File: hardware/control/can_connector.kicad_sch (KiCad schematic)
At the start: 2 parts, among them J401 RJ45_Shielded, J402 RJ45_Shielded

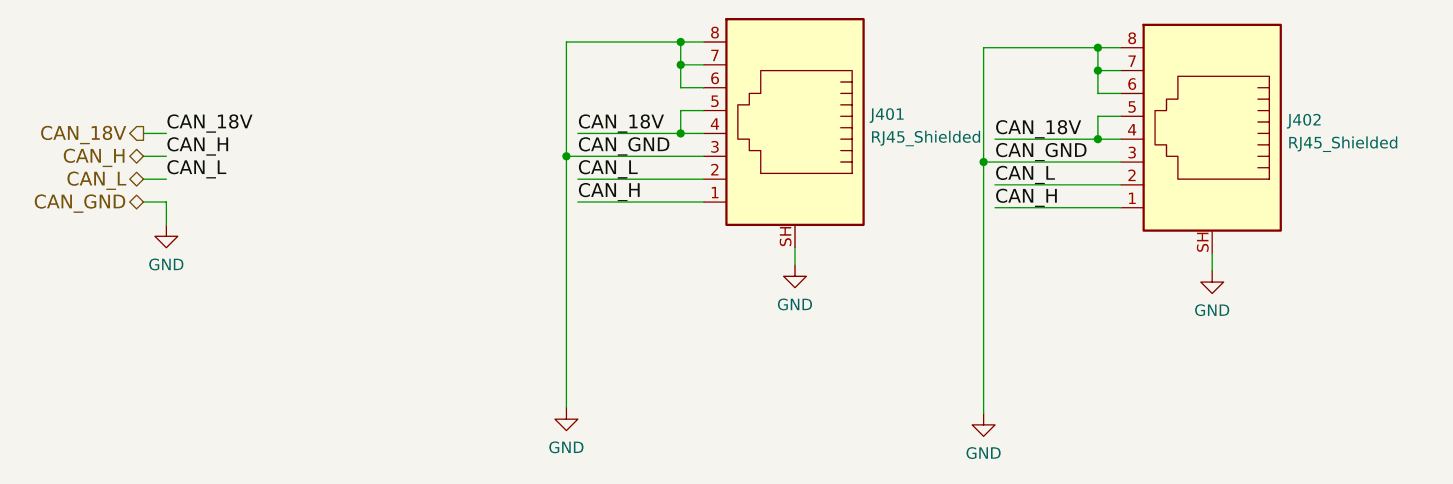
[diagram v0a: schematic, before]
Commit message: Organize schematics per domain
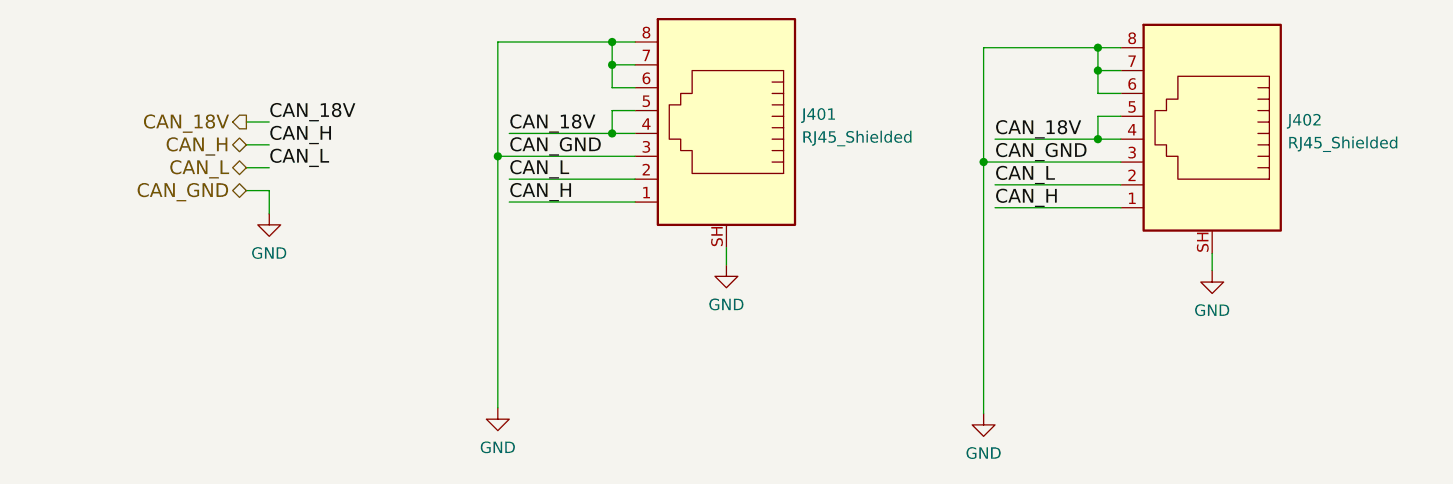
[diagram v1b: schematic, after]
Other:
- company: (none) -> Zenite Solar
- title: (none) -> CAN Connector
- moved on the sheet: J401
